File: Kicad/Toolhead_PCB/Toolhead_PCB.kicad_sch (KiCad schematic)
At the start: 19 parts, among them J1 Conn_02x10_Top_Bottom, J2 Motor, J3 Hotend Fan, J4 Part Cooling Fan, J5 Heater, J6 Thermistor, J7 X-Endstop, J8 Part Cooling Fan, U1 ADXL343, U2 LP2985-3.3

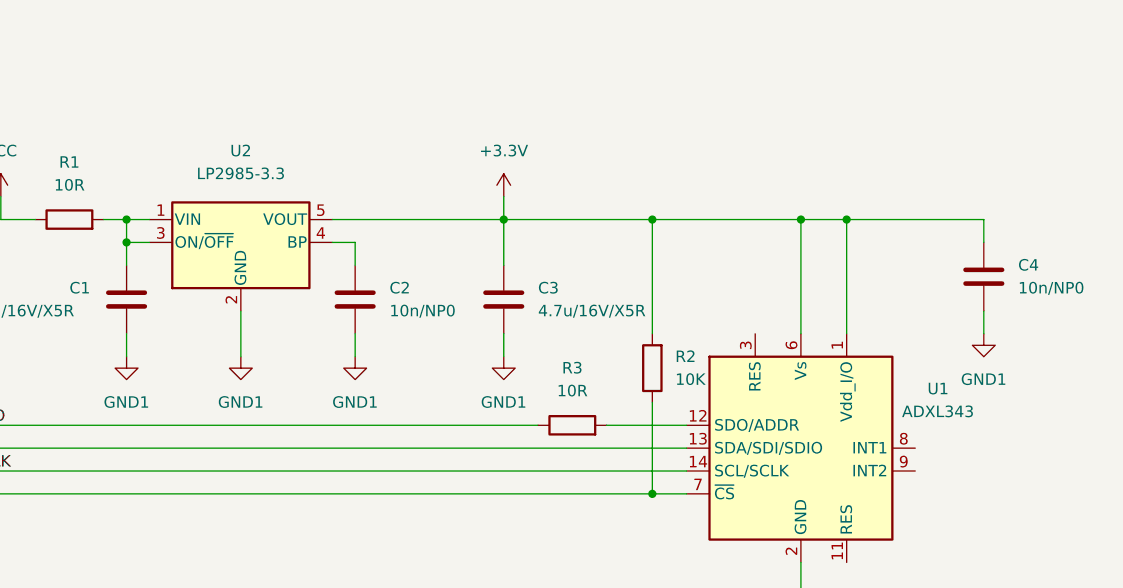
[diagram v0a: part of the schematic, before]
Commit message: Updated part number of ICs
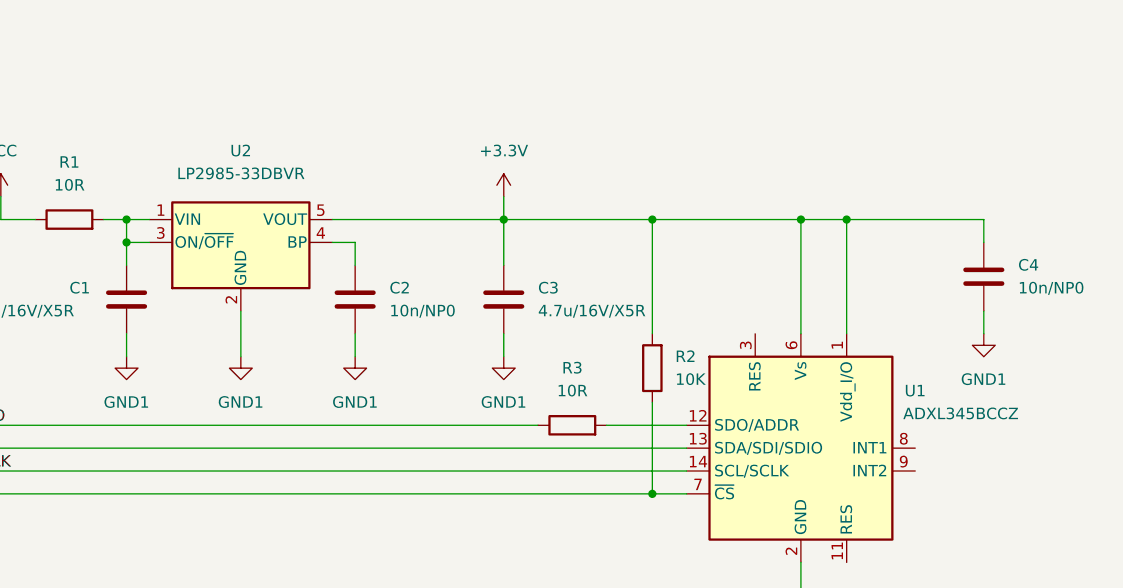
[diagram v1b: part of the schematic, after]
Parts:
- U1: value ADXL343 -> ADXL345BCCZ
- U2: value LP2985-3.3 -> LP2985-33DBVR
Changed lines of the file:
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@@
     (in_bom yes) (on_board yes) (fields_autoplaced)
     (property "Reference" "U2" (id 0) (at 81.28 74.93 0))
-    (property "Value" "LP2985-3.3" (id 1) (at 81.28 77.47 0))
+    (property "Value" "LP2985-33DBVR" (id 1) (at 81.28 77.47 0))
     (property "Footprint" "Package_TO_SOT_SMD:SOT-23-5" (id 2) (at 81.28 76.835 0)
       (effects (font (size 1.27 1.27)) hide)
@@
   )
   (symbol (lib_id "Sensor_Motion:ADXL343") (at 143.51 107.95 0) (unit 1)
-    (in_bom yes) (on_board yes) (fields_autoplaced)
-    (property "Reference" "U1" (id 0) (at 158.75 101.3712 0))
-    (property "Value" "ADXL343" (id 1) (at 158.75 103.9112 0))
+    (in_bom yes) (on_board yes)
+    (property "Reference" "U1" (id 0) (at 156.21 101.6 0))
+    (property "Value" "ADXL345BCCZ" (id 1) (at 161.29 104.14 0))
     (property "Footprint" "Package_LGA:LGA-14_3x5mm_P0.8mm_LayoutBorder1x6y" (id 2) (at 143.51 107.95 0)
       (effects (font (size 1.27 1.27)) hide)
@@
     )
     (path "/d2a5c7fa-a638-42df-b408-a5c6cc7814fa"
-      (reference "U1") (unit 1) (value "ADXL343") (footprint "Package_LGA:LGA-14_3x5mm_P0.8mm_LayoutBorder1x6y")
+      (reference "U1") (unit 1) (value "ADXL345BCCZ") (footprint "Package_LGA:LGA-14_3x5mm_P0.8mm_LayoutBorder1x6y")
     )
     (path "/8d01f112-a20b-4e0d-91e3-0ae5f9deacd3"
-      (reference "U2") (unit 1) (value "LP2985-3.3") (footprint "Package_TO_SOT_SMD:SOT-23-5")
-    )
-  )
+      (reference "U2") (unit 1) (value "LP2985-33DBVR") (footprint "Package_TO_SOT_SMD:SOT-23-5")
+    )
+  )

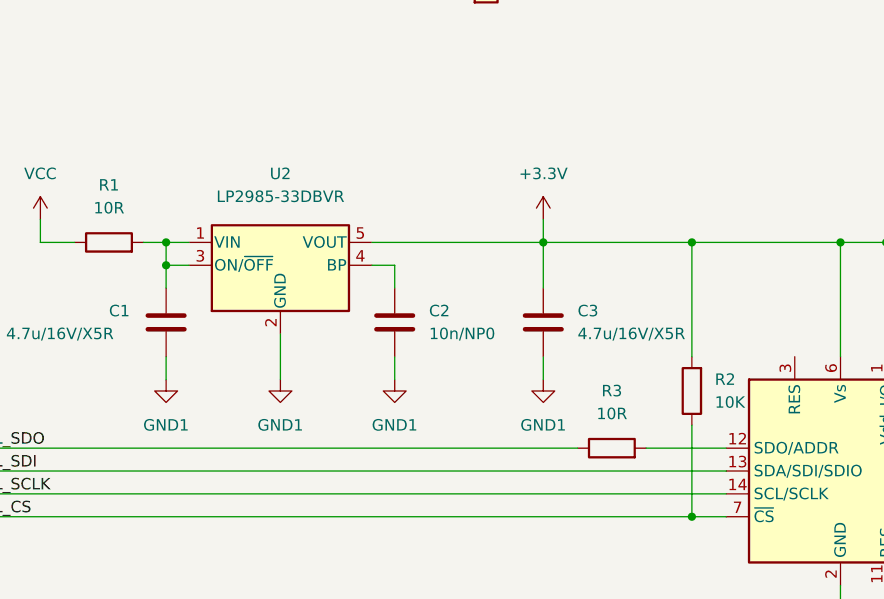
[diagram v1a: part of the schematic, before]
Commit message: Switch LDO to more available part. Migrate to JLCPBC Kicad plugin for maintainability
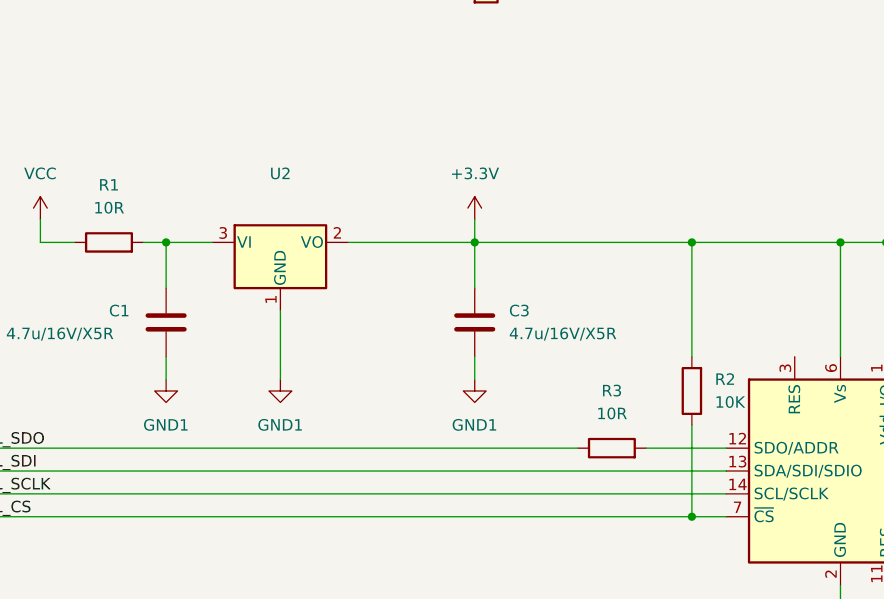
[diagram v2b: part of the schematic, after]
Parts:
- removed C2: 10n/NP0, Capacitor_SMD:C_0603_1608Metric, symbol Device:C
- removed U2: LP2985-33DBVR, Package_TO_SOT_SMD:SOT-23-5, symbol Regulator_Linear:LP2985-3.3
- added U2: (no value), symbol Regulator_Linear:XC6206PxxxMR
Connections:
- net +3V3: now also U2.2 (VO)
- net GND1: now also U2.1 (GND)
- net at C1.1, R1.2: now also U2.3 (VI)
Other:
- moved on the sheet: C3
